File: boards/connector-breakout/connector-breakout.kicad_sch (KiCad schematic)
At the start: 4 parts, among them J1 Harwin M55-7001242R, J2 Conn_01x12, J3 Conn_01x20, J4 Conn_01x20

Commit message: Schematic and footprints done for rev of solar sim connector board
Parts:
- added J6: M55-7101242R, oresat-connectors:J-Harwin-M55-7101242R, symbol Connector_Generic_MountingPin:Conn_01x12_MountingPin
- J1: value Harwin M55-7001242R -> M55-7001242R; footprint oresat-connectors:J-Harwin-M55-7001242R -> oresat-connectors:J-Harwin-M55-7XX1242R; symbol oresat-connectors:Harwin M55-7101242R -> Connector_Generic_MountingPin:Conn_01x12_MountingPin; DIS (none) -> DigiKey; DPN (none) -> 952-3867-1-ND; MFR (none) -> Harwin Inc.; MPN (none) -> M55-7001242R
- J2: value Conn_01x12 -> PRPC012SFAN-RC; DIS (none) -> DigiKey; DPN (none) -> 35-PRPC012SFAN-RC-ND; MFR (none) -> Sullins Connector Solutions; MPN (none) -> PRPC012SFAN-RC
- J3, J4: value Conn_01x20 -> 302-S201; DIS (none) -> DigiKey; DPN (none) -> ED10524-ND; MFR (none) -> On Shore Technology Inc.; MPN (none) -> 302-S201
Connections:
- net CANH: now also J6.10 (Pin_10), J6.9 (Pin_9)
- net CANL: now also J6.11 (Pin_11), J6.12 (Pin_12)
- net GND: now also J1.MP (MountPin), J6.3 (Pin_3), J6.4 (Pin_4), J6.MP (MountPin); no longer J1.SH (Shield)
- net VBUS: now also J6.5 (Pin_5), J6.6 (Pin_6)
- net ~{SD}: now also J6.1 (Pin_1), J6.2 (Pin_2)
- net AUX renamed SM-UART-RX
- net SM-UART-RX: now also J6.8 (Pin_8); no longer J1.7 (Pin_7), J2.7 (Pin_7)
- new net SM-UART-TX: J1.7 (Pin_7), J2.7 (Pin_7), J6.7 (Pin_7)
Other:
- note added: "2.54 mm Breakout"
- note added: "Daisy chaining (Simulator to simulator) cable: Assman H3CCH-2006G"
- note added: "To End/Mid Card plugs (For Solar Module extension cables)"
- note added: "To Solar Module in Solar Simulator"
- company: (none) -> Portland State Aerospace Society
- title: (none) -> Oresat Solar Simulator Connector Board
- moved on the sheet: J2, J3, J4

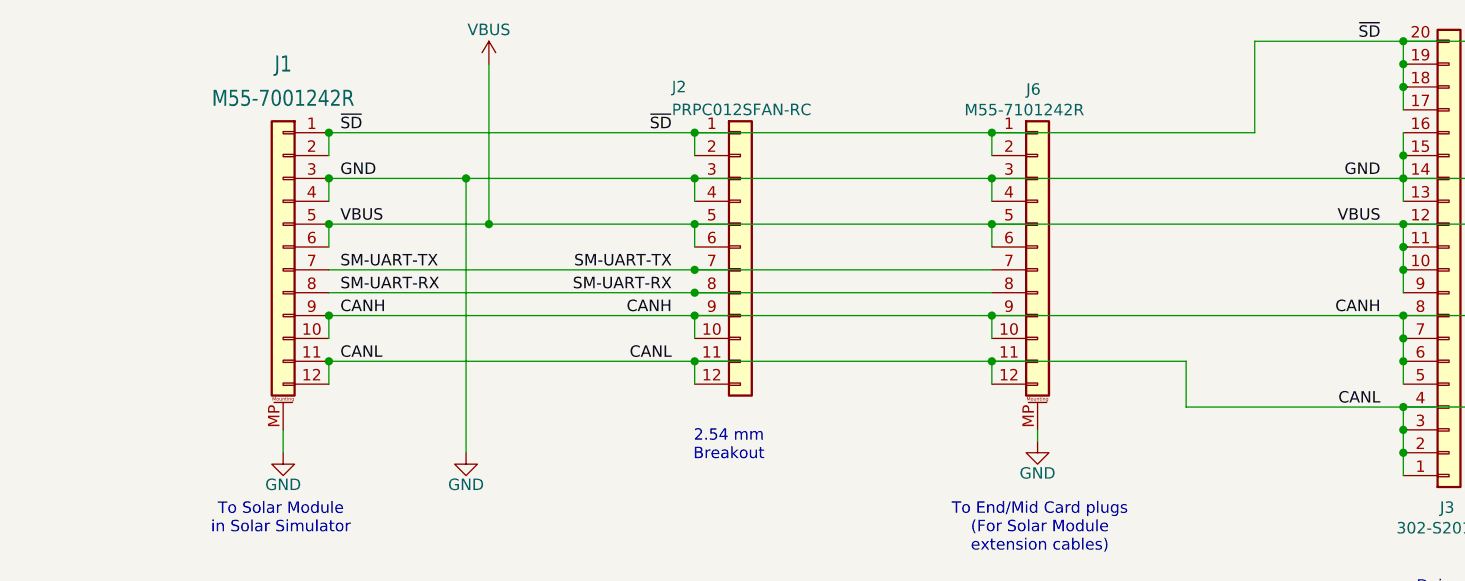
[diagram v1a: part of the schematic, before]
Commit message: Layout updated with connector changes
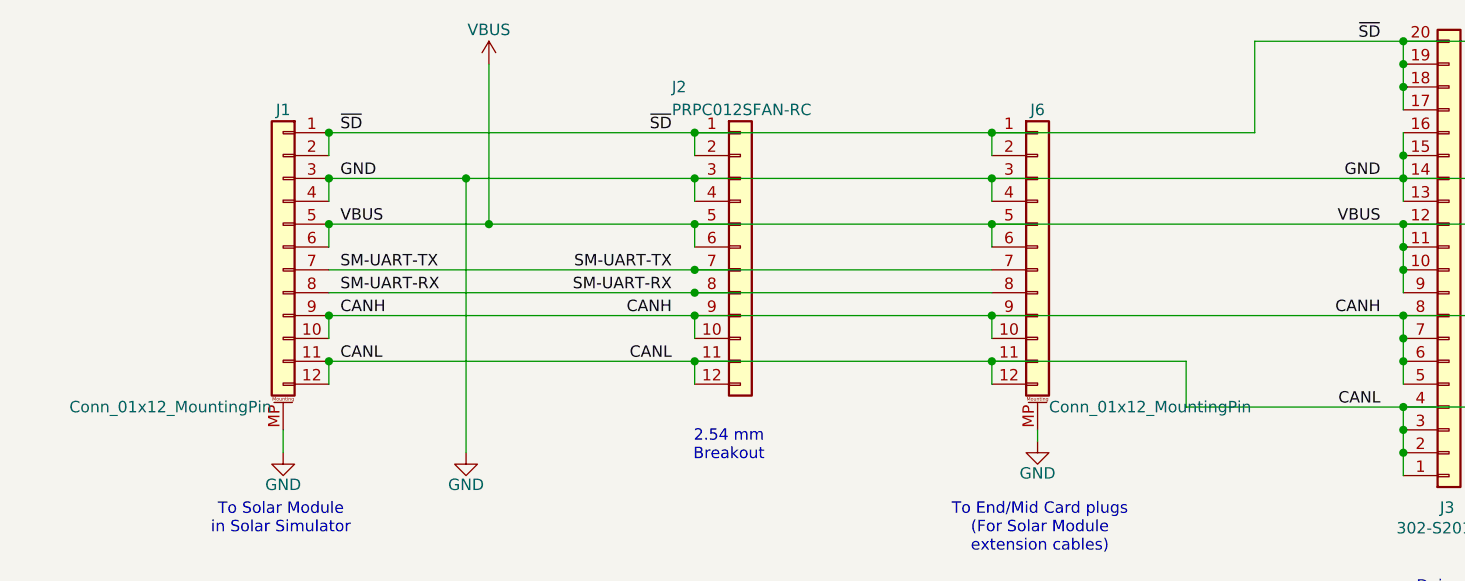
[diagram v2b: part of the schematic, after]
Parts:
- J1: value M55-7001242R -> Conn_01x12_MountingPin; MFR Harwin Inc. -> Harwin
- J6: value M55-7101242R -> Conn_01x12_MountingPin
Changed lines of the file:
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@@
 	(title_block
 		(title "Oresat Solar Simulator Connector Board")
-		(date "2026-09-14")
-		(rev "v1.0")
+		(date "2026-09-16")
+		(rev "v1.1")
 		(company "Portland State Aerospace Society")
 	)
@@
 		(dnp no)
 		(property "Reference" "J1"
-			(at 63.5 67.31 0)
-			(show_name no)
-			(do_not_autoplace no)
-			(effects
-				(font
-					(size 1.778 1.5113)
-				)
-			)
-		)
-		(property "Value" "M55-7001242R"
-			(at 63.5 71.12 0)
-			(show_name no)
-			(do_not_autoplace no)
-			(effects
-				(font
-					(size 1.778 1.5113)
-				)
+			(at 63.5 72.39 0)
+			(show_name no)
+			(do_not_autoplace no)
+			(effects
+				(font
+					(size 1.27 1.27)
+				)
+			)
+		)
+		(property "Value" "Conn_01x12_MountingPin"
+			(at 62.23 105.41 0)
+			(show_name no)
+			(do_not_autoplace no)
+			(effects
+				(font
+					(size 1.27 1.27)
+				)
+				(justify left)
 			)
 		)
@@
 		)
 		(property "Datasheet" "https://cdn.harwin.com/pdfs/C047XX_M55_Archer_Kontrol.pdf"
-			(at 62.23 87.63 0)
-			(hide yes)
-			(show_name no)
-			(do_not_autoplace no)
-			(effects
-				(font
-					(size 1.27 1.27)
-				)
-			)
-		)
-		(property "Description" "Connector Header Surface Mount 12 position 0.050\" (1.27mm)"
+			(at 63.5 87.63 0)
+			(hide yes)
+			(show_name no)
+			(do_not_autoplace no)
+			(effects
+				(font
+					(size 1.27 1.27)
+				)
+			)
+		)
+		(property "Description" "Generic connectable mounting pin connector, single row, 01x12, script generated (kicad-library-utils/schlib/autogen/connector/)"
 			(at 63.5 87.63 0)
 			(hide yes)
@@
 			)
 		)
-		(property "MFR" "Harwin Inc."
+		(property "MFR" "Harwin"
 			(at 63.5 87.63 0)
 			(hide yes)
@@
 		(dnp no)
 		(property "Reference" "J6"
-			(at 146.05 70.866 0)
-			(show_name no)
-			(do_not_autoplace no)
-			(effects
-				(font
-					(size 1.27 1.27)
-				)
-				(justify left bottom)
-			)
-		)
-		(property "Value" "M55-7101242R"
-			(at 139.192 73.152 0)
-			(show_name no)
-			(do_not_autoplace no)
-			(effects
-				(font
-					(size 1.27 1.27)
-				)
-				(justify left bottom)
+			(at 147.32 72.39 0)
+			(show_name no)
+			(do_not_autoplace no)
+			(effects
+				(font
+					(size 1.27 1.27)
+				)
+			)
+		)
+		(property "Value" "Conn_01x12_MountingPin"
+			(at 148.59 105.41 0)
+			(show_name no)
+			(do_not_autoplace no)
+			(effects
+				(font
+					(size 1.27 1.27)
+				)
+				(justify left)
 			)
 		)
@@
 			)
 		)
-		(property "Description" "Connector Header Surface Mount, Right Angle 12 position 0.050\" (1.27mm)"
+		(property "Description" "Generic connectable mounting pin connector, single row, 01x12, script generated (kicad-library-utils/schlib/autogen/connector/)"
 			(at 147.32 87.63 0)
 			(hide yes)

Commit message: Solar Simulator Connector Board v1.1
Recovered missing holes, added fiducials, brought up to modern standards with stackup, makefile, and readme, fixed stiching and date, checked BOM, should be good to go.
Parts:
- added FID1, FID2, FID3: Fiducial, Fiducial:Fiducial_1mm_Mask2mm, symbol Mechanical:Fiducial
- added H1, H2: MountingHole, MountingHole:MountingHole_2.2mm_M2_ISO14580, symbol Mechanical:MountingHole
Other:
- note added: "Copy of End/Mid Card plugs (For Solar Module extension cables)"
- note added: "WARNING: DOES NOT HAVE UART LINES!!"
- note removed: "To End/Mid Card plugs (For Solar Module extension cables)"
